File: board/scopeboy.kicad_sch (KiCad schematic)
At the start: 110 parts, among them J1 USB_C_Receptacle_USB2.0_16P, J2 SM03B-SRSS-TB, J3 SM03B-SRSS-TB, J4 Conn_01x10, J5 SM04B-SRSS-TB, J6 HDMI_A, J8 Conn_01x02, J9 Conn_01x08, SW1 SW_Push, SW2 SW_Push, SW3 RotaryEncoder_Switch, U1 W25Q128JVS, U17 TLV62568DBVR, U18 MT3608 (TPS61023DRLR), U2 DNF, U4 RP2350_80QFN, U5 TPS2116DRL, U6 LM27762, U7 ADC08060, Y1 ABM8-272-T3

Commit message: Updated the board stackup
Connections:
- net +3V3 is gone; now on net +3.3V: C1.1, C13.1, C14.1, C15.1, C16.1, C17.1, C18.1, C19.1, C2.1, C20.1, C21.1, C22.1, C36.2, C38.2, C5.1, J4.2 (Pin_2), J5.2 (Pin_2), R10.1, R14.2, R15.2, R4.1, R5.1, U1.8 (VCC), U2.8 (VCC), U4.15 (IOVDD), U4.24 (IOVDD), U4.29 (IOVDD), U4.41 (IOVDD), U4.5 (IOVDD), U4.50 (IOVDD), U4.59 (ADC_AVDD), U4.60 (IOVDD), U4.64 (VREG_VIN), U4.68 (USB_OTP_VDD), U4.69 (QSPI_IOVDD), U4.76 (IOVDD), U7.18 (DRVD)
- net GPIO26 is gone; now on net Backlight: U4.27 (GPIO26)
- net GPIO27 is gone; now on net D/C: U4.28 (GPIO27)
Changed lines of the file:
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@@
 		)
 	)
+	(label "Backlight"
+		(at 250.19 177.8 180)
+		(effects
+			(font
+				(size 1.27 1.27)
+			)
+			(justify right bottom)
+		)
+	)
 	(label "MISO"
 		(at 410.21 39.37 0)
@@
 		)
 	)
+	(label "D{slash}C"
+		(at 250.19 180.34 180)
+		(effects
+			(font
+				(size 1.27 1.27)
+			)
+			(justify right bottom)
+		)
+	)
 	(label "SD_D0"
 		(at 250.19 132.08 180)
@@
 		)
 	)
-	(label "GPIO27"
-		(at 250.19 180.34 180)
-		(effects
-			(font
-				(size 1.27 1.27)
-			)
-			(justify right bottom)
-		)
-	)
 	(label "QSPI_SD1"
 		(at 152.4 129.54 0)
@@
 		)
 	)
-	(label "GPIO26"
-		(at 250.19 177.8 180)
-		(effects
-			(font
-				(size 1.27 1.27)
-			)
-			(justify right bottom)
-		)
-	)
 	(global_label "CLK"
 		(shape input)
@@
 			)
 		)
-		(property "Value" "+3V3"
+		(property "Value" "+3.3V"
 			(at 67.691 99.1108 0)
 			(effects
@@
 	)
 	(symbol
-		(lib_id "power:+3V3")
-		(at 219.71 59.69 0)
-		(unit 1)
-		(exclude_from_sim no)
-		(in_bom yes)
-		(on_board yes)
-		(dnp no)
-		(property "Reference" "#PWR027"
-			(at 219.71 63.5 0)
-			(effects
-				(font
-					(size 1.27 1.27)
-				)
-				(hide yes)
-			)
-		)
-		(property "Value" "+3V3"
-			(at 220.091 55.2958 0)
-			(effects
-				(font
-					(size 1.27 1.27)
-				)
-			)
-		)
-		(property "Footprint" ""
-			(at 219.71 59.69 0)
-			(effects
-				(font
-					(size 1.27 1.27)
-				)
-				(hide yes)
-			)
-		)
-		(property "Datasheet" ""
-			(at 219.71 59.69 0)
-			(effects
-				(font
-					(size 1.27 1.27)
-				)
-				(hide yes)
-			)
-		)
-		(property "Description" ""
-			(at 219.71 59.69 0)
-			(effects
-				(font
-					(size 1.27 1.27)
-				)
-			)
-		)
-		(pin "1"
-		)
-		(instances
-			(project "scopeboy"
-				(path "/94683f5c-9cd9-448e-be96-9792537b5cb8"
-					(reference "#PWR027")
-					(unit 1)
-				)
-			)
-		)
-	)
-	(symbol
 		(lib_id "Device:C")
 		(at 251.46 66.04 0)
@@
 			)
 		)
-		(property "Value" "+3V3"
+		(property "Value" "+3.3V"
 			(at 281.051 140.3858 0)
 			(effects
@@
 			)
 		)
-		(property "Value" "+3V3"
+		(property "Value" "+3.3V"
 			(at 489.331 349.9358 0)
 			(effects
@@
 			)
 		)
-		(property "Value" "+3V3"
+		(property "Value" "+3.3V"
 			(at 477.901 349.9358 0)
 			(effects
@@
 			)
 		)
-		(property "Value" "+3V3"
+		(property "Value" "+3.3V"
 			(at 451.231 323.2658 0)
 			(effects
@@
 			)
 		)
-		(property "Value" "+3V3"
+		(property "Value" "+3.3V"
 			(at 68.961 158.1658 0)
 			(effects
@@
 			)
 		)
-		(property "Value" "+3V3"
+		(property "Value" "+3.3V"
 			(at 486.41 49.53 0)
 			(effects
@@
 			)
 		)
-		(property "Value" "+3V3"
+		(property "Value" "+3.3V"
 			(at 398.78 74.93 0)
 			(effects
@@
 			)
 		)
-		(property "Value" "+3V3"
+		(property "Value" "+3.3V"
 			(at 425.45 49.53 0)
 			(effects
@@
 			)
 		)
-		(property "Value" "+3V3"
+		(property "Value" "+3.3V"
 			(at 387.35 74.93 0)
 			(effects
@@
 	)
 	(symbol
-		(lib_id "power:+3V3")
-		(at 107.95 87.63 0)
+		(lib_id "power:GND")
+		(at 482.6 58.42 0)
 		(unit 1)
 		(exclude_from_sim no)
@@
 		(on_board yes)
 		(dnp no)
-		(property "Reference" "#PWR013"
-			(at 107.95 91.44 0)
+		(property "Reference" "#PWR070"
+			(at 482.6 64.77 0)
 			(effects
 				(font
@@
 			)
 		)
-		(property "Value" "+3V3"
-			(at 108.331 83.2358 0)
+		(property "Value" "GND"
+			(at 482.727 62.8142 0)
 			(effects
 				(font
@@
 		)
 		(property "Footprint" ""
-			(at 107.95 87.63 0)
+			(at 482.6 58.42 0)
 			(effects
 				(font
@@
 		)
 		(property "Datasheet" ""
-			(at 107.95 87.63 0)
+			(at 482.6 58.42 0)
 			(effects
 				(font
@@
 		)
 		(property "Description" ""
-			(at 107.95 87.63 0)
+			(at 482.6 58.42 0)
 			(effects
 				(font
 					(size 1.27 1.27)
 				)
+				(hide yes)
 			)
 		)
@@
 			(project "scopeboy"
 				(path "/94683f5c-9cd9-448e-be96-9792537b5cb8"
-					(reference "#PWR013")
+					(reference "#PWR070")
 					(unit 1)
 				)
@@
 	)
 	(symbol
-		(lib_id "power:GND")
-		(at 482.6 58.42 0)
+		(lib_id "power:+3.3VA")
+		(at 219.71 59.69 0)
 		(unit 1)
 		(exclude_from_sim no)
@@
 		(on_board yes)
 		(dnp no)
-		(property "Reference" "#PWR070"
-			(at 482.6 64.77 0)
+		(property "Reference" "#PWR027"
+			(at 219.71 63.5 0)
 			(effects
 				(font
@@
 			)
 		)
-		(property "Value" "GND"
-			(at 482.727 62.8142 0)
+		(property "Value" "+3.3V"
+			(at 217.678 55.118 0)
 			(effects
 				(font
@@
 		)
 		(property "Footprint" ""
-			(at 482.6 58.42 0)
+			(at 219.71 59.69 0)
 			(effects
 				(font
@@
 		)
 		(property "Datasheet" ""
-			(at 482.6 58.42 0)
+			(at 219.71 59.69 0)
 			(effects
 				(font
@@
 		)
 		(property "Description" ""
-			(at 482.6 58.42 0)
+			(at 219.71 59.69 0)
 			(effects
 				(font
@@
 			(project "scopeboy"
 				(path "/94683f5c-9cd9-448e-be96-9792537b5cb8"
-					(reference "#PWR070")
+					(reference "#PWR027")
 					(unit 1)
 				)
@@
 					(unit 1)
 				)
+			)
+		)
+	)
+	(symbol
+		(lib_id "power:+3.3VA")
+		(at 107.95 87.63 0)
+		(unit 1)
+		(exclude_from_sim no)
+		(in_bom yes)
+		(on_board yes)
+		(dnp no)
+		(property "Reference" "#PWR013"
+			(at 107.95 91.44 0)
+			(effects
+				(font
+					(size 1.27 1.27)
+				)
+				(hide yes)
+			)
+		)
+		(property "Value" "+3.3V"
+			(at 105.918 83.058 0)
+			(effects
+				(font
+					(size 1.27 1.27)
+				)
+			)
+		)
+		(property "Footprint" ""
+			(at 107.95 87.63 0)
+			(effects
+				(font
+					(size 1.27 1.27)
+				)
+				(hide yes)
+			)
+		)
+		(property "Datasheet" ""
+			(at 107.95 87.63 0)
+			(effects
+				(font
+					(size 1.27 1.27)
+				)
+				(hide yes)
+			)
+		)
+		(property "Description" ""
+			(at 107.95 87.63 0)
+			(effects
+				(font
+					(size 1.27 1.27)
+				)
+				(hide yes)
+			)
+		)
+		(pin "1"
+		)
+		(instances
+			(project "scopeboy"
+				(path "/94683f5c-9cd9-448e-be96-9792537b5cb8"
+					(reference "#PWR013")
+					(unit 1)
+				)

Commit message: Removed TODO comments
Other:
- note removed: "TODO connect all the GPIO pins"
- note removed: "TODO do we need to connect the 5V for HDMI?"
- note removed: "TODO double check these based on https://learn.adafruit.com/adafruit-rp2350-22-pin-fpc-hstx-to-dvi-adapter/pinouts"
- note removed: "TODO this symbol needs to be updated to actually match the TPS61023DRLR"
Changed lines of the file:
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@@
-		)
-	)
-	(text "TODO connect all the GPIO pins"
-		(exclude_from_sim no)
-		(at 270.51 171.196 0)
-		(effects
-			(font
-				(size 1.27 1.27)
-			)
 		)
 	)
@@
 			)
 			(justify left bottom)
-		)
-	)
-	(text "TODO do we need to connect the 5V for HDMI?"
-		(exclude_from_sim no)
-		(at 531.876 70.866 0)
-		(effects
-			(font
-				(size 1.27 1.27)
-			)
-		)
-	)
-	(text "TODO double check these based on\nhttps://learn.adafruit.com/adafruit-rp2350-22-pin-fpc-hstx-to-dvi-adapter/pinouts"
-		(exclude_from_sim no)
-		(at 573.532 80.772 0)
-		(effects
-			(font
-				(size 1.27 1.27)
-			)
 		)
 	)
@@
 		)
 	)
-	(text "TODO this symbol needs to be updated to actually match the TPS61023DRLR"
-		(exclude_from_sim no)
-		(at 451.358 202.692 0)
-		(effects
-			(font
-				(size 1.27 1.27)
-			)
-		)
-	)

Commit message: Production version of board
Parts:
- C1, C12, C13, C14, C15, C16, C18, C19, C20, C21, C22, C8: MFR. Part # (none) -> AC0402JRNPO9BN100
- C10, C11, C5, C7: MFR. Part # (none) -> CL05A475MP5NRNC
- C17, C53, C54: MFR. Part # (none) -> CL21A106KOQNNNE
- C2, R1, R3, R4, R5: now not fitted; now left out of the parts list
- C3, C4: MFR. Part # (none) -> GJM1555C1H150GB01D
- C37, C6: MFR. Part # (none) -> CL21A226MQQNNNE
- D5: MFR. Part # (none) -> SS14
- H1, H2, H3, H4: now not fitted
- J4, J9, U2: now left out of the parts list
- J6: MFR. Part # (none) -> 2086581001
- L1: MFR. Part # (none) -> SRN4018TA-3R3M
- L2: MFR. Part # (none) -> SRN4018TA-4R7M
- L3: MFR. Part # (none) -> SRN4018-2R2M
- R10: MFR. Part # (none) -> RC0402JR-0733RL
- R11, R8, R9: MFR. Part # (none) -> CRCW04021K00FKED
- R12, R13: MFR. Part # (none) -> RC0402JR-0727RL
- R14, R15, R19, R32, R49, R52: MFR. Part # (none) -> RC0603FR-0710KL
- R2: MFR. Part # (none) -> RC0402JR-070RL
- R24, R25, R26, R27, R28, R29, R30, R31: MFR. Part # (none) -> CRGCQ0603J220R
- R48, R54, R55: MFR. Part # (none) -> RC0603FR-07100KL
- R50: MFR. Part # (none) -> RC0603FR-0747KL
- R51: MFR. Part # (none) -> RMCF0603FT73K2
- R53: MFR. Part # (none) -> CRCW0603453KFKEAC
- SW3: MFR. Part # (none) -> PEC11L4115FS0020
- U1: MFR. Part # (none) -> W25Q128JVS
- U17: MFR. Part # (none) -> TLV62568DBVR
- U18: MFR. Part # (none) -> MT3608
- U4: MFR. Part # (none) -> RP2354B
- U5: MFR. Part # (none) -> TPS2116DRLR
- U7: LCSC Part # C701580 -> C701069; MFR. Part # ADC08060CIMTX/NOPB -> TI ADC08060CIMT/NOPB
- Y1: MFR. Part # (none) -> ABM8-272-T3

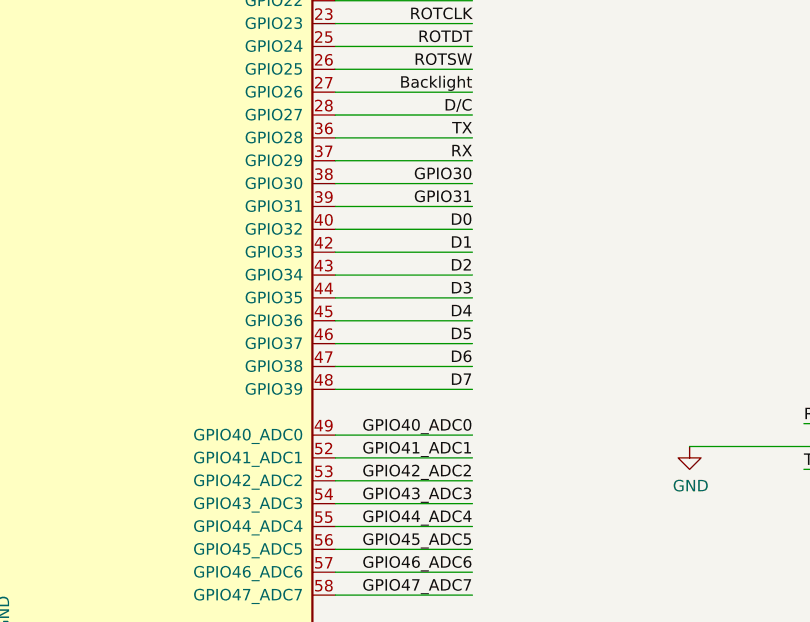
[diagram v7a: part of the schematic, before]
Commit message: Fixing reset on TFT
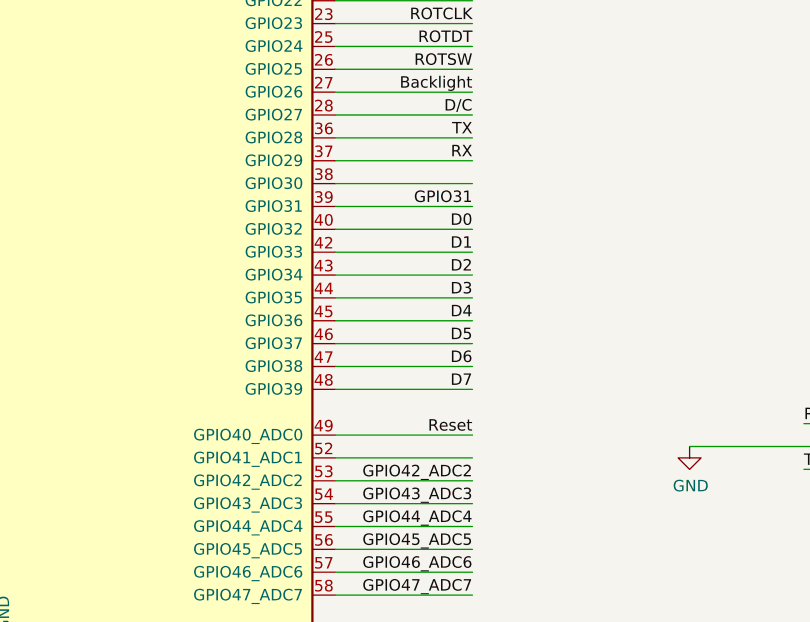
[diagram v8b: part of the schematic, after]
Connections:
- net GPIO40_ADC0 is gone; now on net Reset: U4.49 (GPIO40_ADC0)
- net GPIO30: no longer names the net of U4.38 (GPIO30)
- net GPIO41_ADC1: no longer names the net of U4.52 (GPIO41_ADC1)
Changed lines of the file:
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@@
 	(title_block
 		(title "Scopeboy")
-		(date "2026-04-19")
-		(rev "V1.0")
+		(date "2026-05-12")
+		(rev "V1.1")
 		(company "Cornell University Electrical and Computer Engineering")
 		(comment 1 "Jenny List")
@@
 		)
 	)
-	(label "GPIO40_ADC0"
-		(at 250.19 215.9 180)
-		(effects
-			(font
-				(size 1.27 1.27)
-			)
-			(justify right bottom)
-		)
-	)
 	(label "D5"
 		(at 250.19 205.74 180)
@@
 		)
 	)
-	(label "GPIO41_ADC1"
-		(at 250.19 218.44 180)
-		(effects
-			(font
-				(size 1.27 1.27)
-			)
-			(justify right bottom)
-		)
-	)
 	(label "XOUT"
 		(at 152.4 152.4 0)
@@
 		)
 	)
-	(label "GPIO30"
-		(at 250.19 187.96 180)
-		(effects
-			(font
-				(size 1.27 1.27)
-			)
-			(justify right bottom)
-		)
-	)
 	(label "CDSD"
 		(at 350.52 135.89 180)
@@
 		(effects
 			(font
+				(size 1.27 1.27)
+			)
+			(justify right bottom)
+		)
+	)
+	(label "Reset"
+		(at 250.19 215.9 180)
+		(effects
+			(font
